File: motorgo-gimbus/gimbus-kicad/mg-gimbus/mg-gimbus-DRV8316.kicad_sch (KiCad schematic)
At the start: 9 parts, among them U12 DRV8316CRRGFR

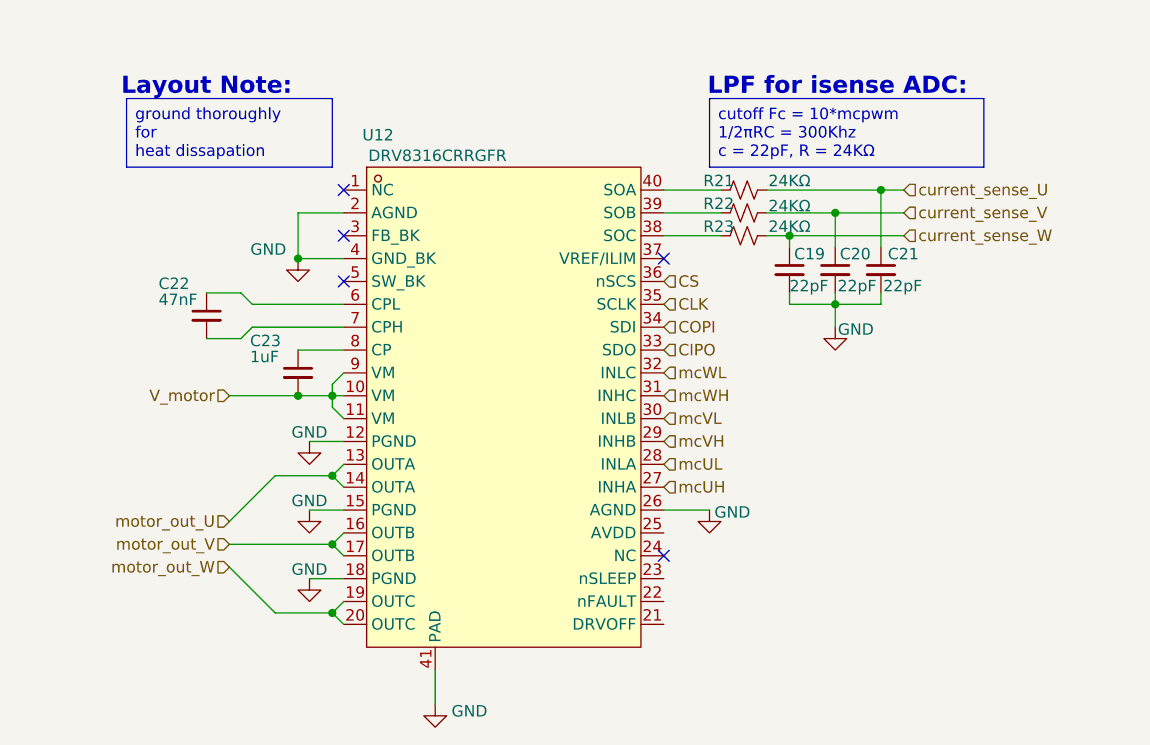
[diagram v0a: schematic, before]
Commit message: update motor controls schema
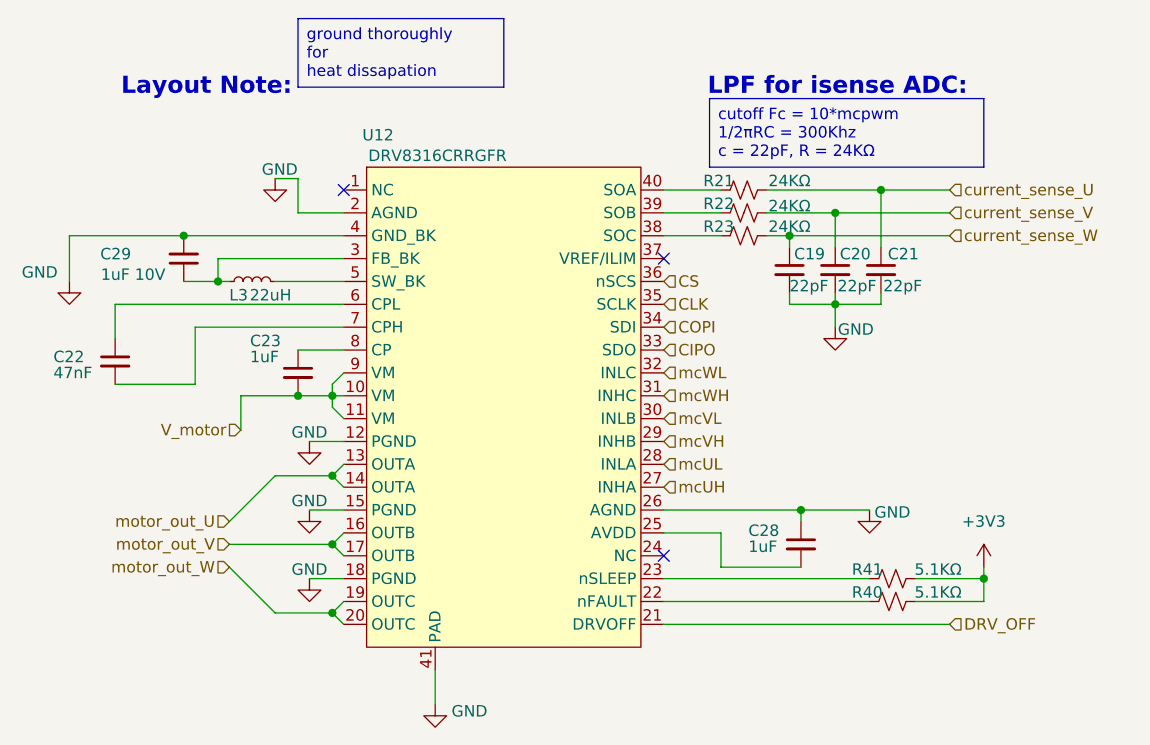
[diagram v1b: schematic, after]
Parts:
- added C28: 1uF, symbol Device:C_Small
- added C29: 1uF 10V, symbol Device:C_Small
- added L3: 22uH, symbol Device:L_Small
- added R40, R41: 5.1KΩ, symbol Device:R_Small_US
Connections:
- net GND: now also C28.1, C29.2
- net DRV_OFF: now reaches U12.21 (DRVOFF)
- net at U12.22 (nFAULT): now also R40.1
- net at U12.23 (nSLEEP): now also R41.1
- net at U12.25 (AVDD): now also C28.2
- net at U12.3 (FB_BK): now also C29.1, L3.1
- net at U12.5 (SW_BK): now also L3.2
- new net +3V3: R40.2, R41.2
- no-connect marks 5 -> 3
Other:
- moved on the sheet: C22

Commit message: incremental layout progress
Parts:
- C19, C20, C21: footprint (none) -> Capacitor_SMD:C_0402_1005Metric; LCSC Part (none) -> C76960
- C22: footprint (none) -> Capacitor_SMD:C_0402_1005Metric; LCSC Part (none) -> C82219
- C23, C28: value 1uF -> 1uF 50V; footprint (none) -> Capacitor_SMD:C_0805_2012Metric; LCSC Part (none) -> C28323
- C29: value 1uF 10V -> 1uF 50V; footprint (none) -> Capacitor_SMD:C_0805_2012Metric; LCSC Part (none) -> C28323
- L3: footprint (none) -> Inductor_SMD:L_0603_1608Metric; LCSC Part (none) -> C383393
- R21, R22, R23: footprint (none) -> Resistor_SMD:R_0402_1005Metric; LCSC Part (none) -> C25769
- R40, R41: footprint (none) -> Resistor_SMD:R_0402_1005Metric; LCSC Part (none) -> C25905
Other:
- company: (none) -> MotorGo LLC
- title: (none) -> MotorGo Gimbus
